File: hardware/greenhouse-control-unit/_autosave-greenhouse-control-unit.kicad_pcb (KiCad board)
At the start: 4 copper layers, 150 x 90 mm, 53 parts, among them J1 Buck_Conn_01x01_Female, J10 Conn_ESP32_DevKitV1_Female, J12 Conn_01x05_Female, J13 Beep_Jumper, J15 Conn_01x05_Female, J16 Conn_01x05_Female, J2 Buck_Conn_01x01_Female, J3 Buck_Conn_01x01_Female, J4 Buck_Conn_01x01_Female, J5 Molex_KK-396_01x02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

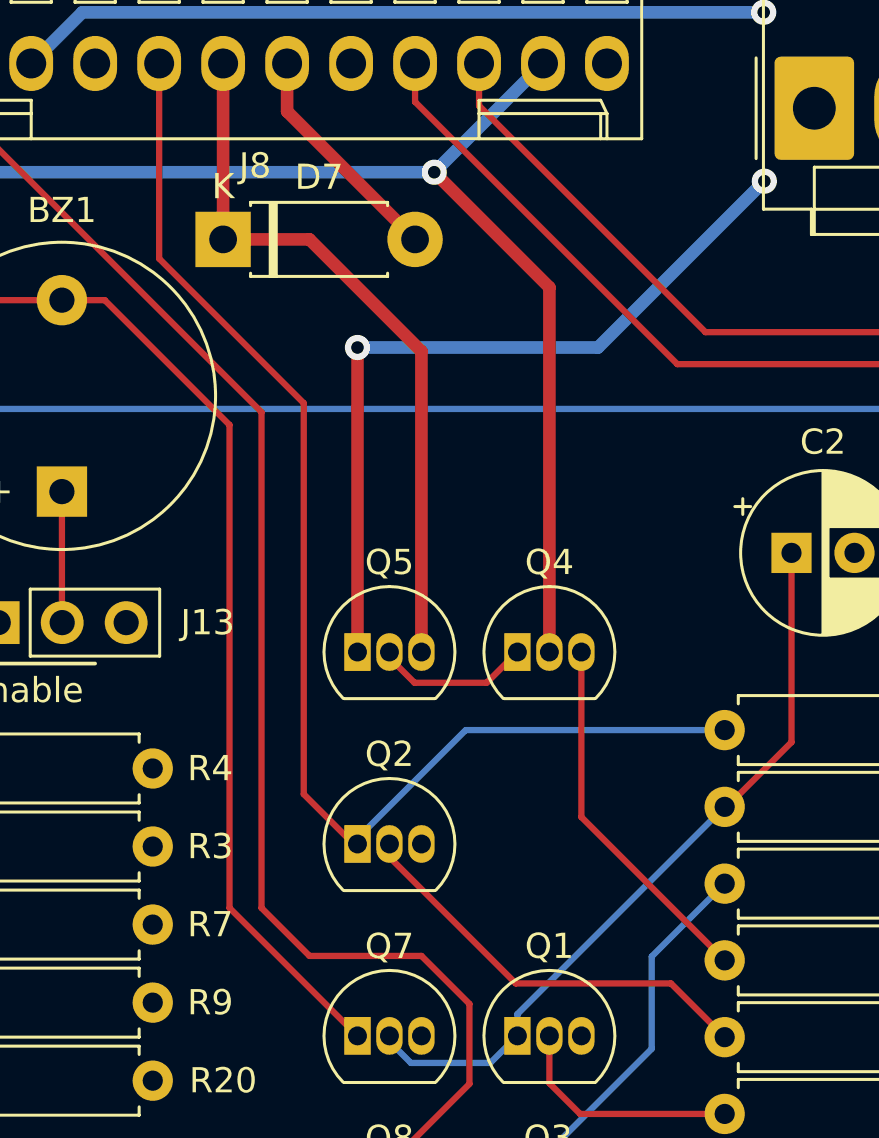
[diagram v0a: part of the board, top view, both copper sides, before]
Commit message: Reintroduced battery relay
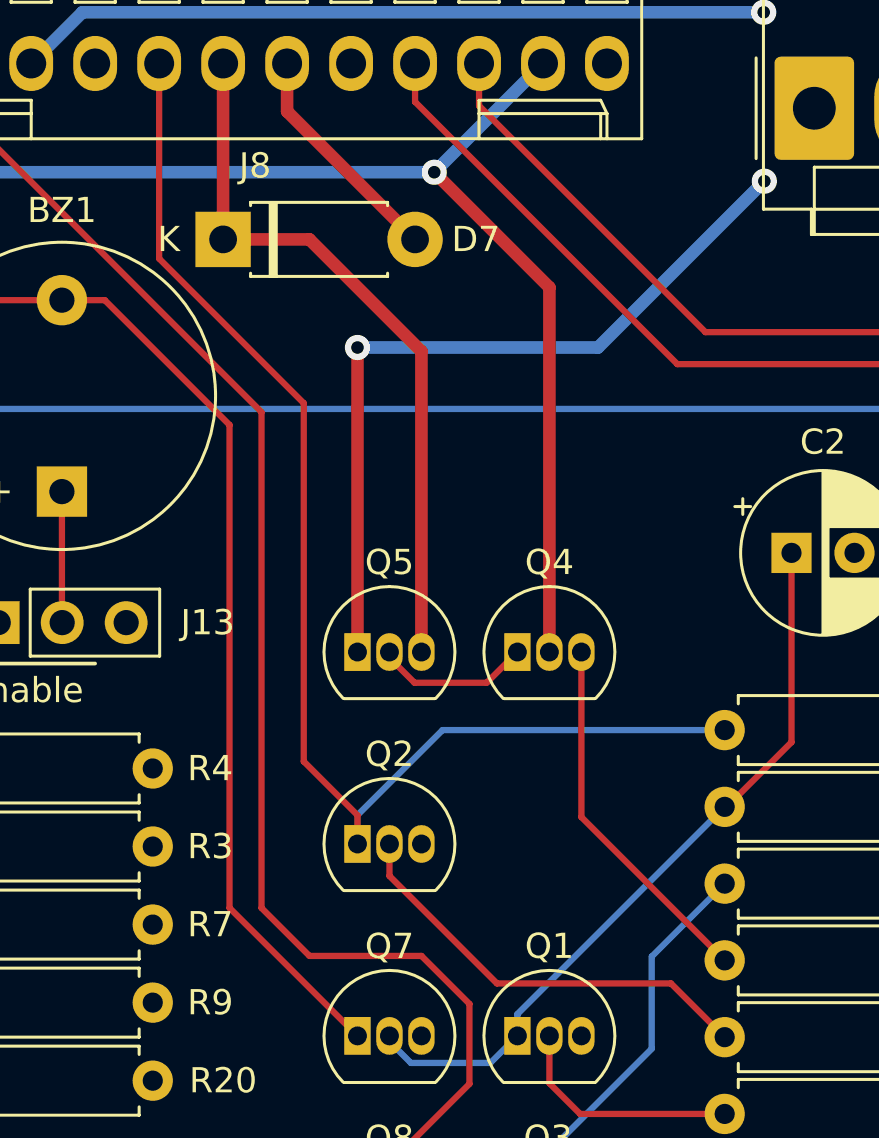
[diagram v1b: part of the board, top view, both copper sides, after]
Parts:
- Q5: value BC327 -> 2N3906
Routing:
- net /PsuRelayNC_IN: track 50.0 -> 50.5 mm
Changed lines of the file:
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@@
     (property "Sheetname" "")
     (attr through_hole)
-    (fp_text reference "D7" (at 3.81 -2.47) (layer "F.SilkS")
+    (fp_text reference "D7" (at 10.033 0) (layer "F.SilkS")
       (effects (font (size 1 1) (thickness 0.15)))
     )
@@
       (effects (font (size 1 1) (thickness 0.15)))
     )
-    (fp_text user "K" (at 0 -2.1) (layer "F.SilkS")
+    (fp_text user "K" (at -2.159 0) (layer "F.SilkS")
       (effects (font (size 1 1) (thickness 0.15)))
     )
@@
       (effects (font (size 1 1) (thickness 0.15)))
     )
-    (fp_text value "BC327" (at 1.27 2.79) (layer "F.Fab")
+    (fp_text value "2N3906" (at 1.27 2.79) (layer "F.Fab")
       (effects (font (size 1 1) (thickness 0.15)))
     )
@@
   (segment (start 119.9896 85.1408) (end 114.3 79.4512) (width 0.25) (layer "F.Cu") (net 75))
   (segment (start 114.3 79.4512) (end 114.3 72.898) (width 0.25) (layer "F.Cu") (net 75))
-  (segment (start 117.856 86.0552) (end 111.695111 86.0552) (width 0.25) (layer "F.Cu") (net 76))
-  (segment (start 111.695111 86.0552) (end 106.68 81.040089) (width 0.25) (layer "F.Cu") (net 76))
+  (segment (start 117.856 86.0552) (end 110.9472 86.0552) (width 0.25) (layer "F.Cu") (net 76))
+  (segment (start 110.9472 86.0552) (end 106.68 81.788) (width 0.25) (layer "F.Cu") (net 76))
   (segment (start 119.9896 88.1888) (end 117.856 86.0552) (width 0.25) (layer "F.Cu") (net 76))
+  (segment (start 106.68 81.788) (end 106.68 81.040089) (width 0.25) (layer "F.Cu") (net 76))
+  (segment (start 97.536 57.277) (end 103.2764 63.0174) (width 0.25) (layer "F.Cu") (net 77))
+  (segment (start 103.2764 77.2414) (end 105.41 79.375) (width 0.25) (layer "F.Cu") (net 77))
+  (segment (start 103.2764 63.0174) (end 103.2764 77.2414) (width 0.25) (layer "F.Cu") (net 77))
   (segment (start 97.536 50.292) (end 97.536 57.277) (width 0.25) (layer "F.Cu") (net 77))
-  (segment (start 103.2764 78.540802) (end 105.41 80.674402) (width 0.25) (layer "F.Cu") (net 77))
-  (segment (start 103.2764 63.0174) (end 103.2764 78.540802) (width 0.25) (layer "F.Cu") (net 77))
-  (segment (start 97.536 57.277) (end 103.2764 63.0174) (width 0.25) (layer "F.Cu") (net 77))
-  (segment (start 109.7062 75.9968) (end 105.41 80.293) (width 0.25) (layer "B.Cu") (net 77))
-  (segment (start 119.9896 75.9968) (end 109.7062 75.9968) (width 0.25) (layer "B.Cu") (net 77))
+  (segment (start 105.41 79.375) (end 105.41 80.674402) (width 0.25) (layer "F.Cu") (net 77))
+  (segment (start 119.9896 75.9968) (end 108.7882 75.9968) (width 0.25) (layer "B.Cu") (net 77))
+  (segment (start 105.41 79.375) (end 105.41 80.293) (width 0.25) (layer "B.Cu") (net 77))
+  (segment (start 108.7882 75.9968) (end 105.41 79.375) (width 0.25) (layer "B.Cu") (net 77))
   (zone locked (net 30) (net_name "+12V") (layer "In1.Cu") (hatch edge 0.508)
     (connect_pads yes (clearance 0.508))
